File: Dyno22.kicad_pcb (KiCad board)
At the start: 2 copper layers, 160 x 110 mm, 49 parts, among them J2 Display, J3 Pwr Output, J4 BPM & Sensors, J5 Pwr Input, J7 UART, SW1 SW_DPST_x2, U1 TS2937CW50, U2 LM324, U3 74HC4052

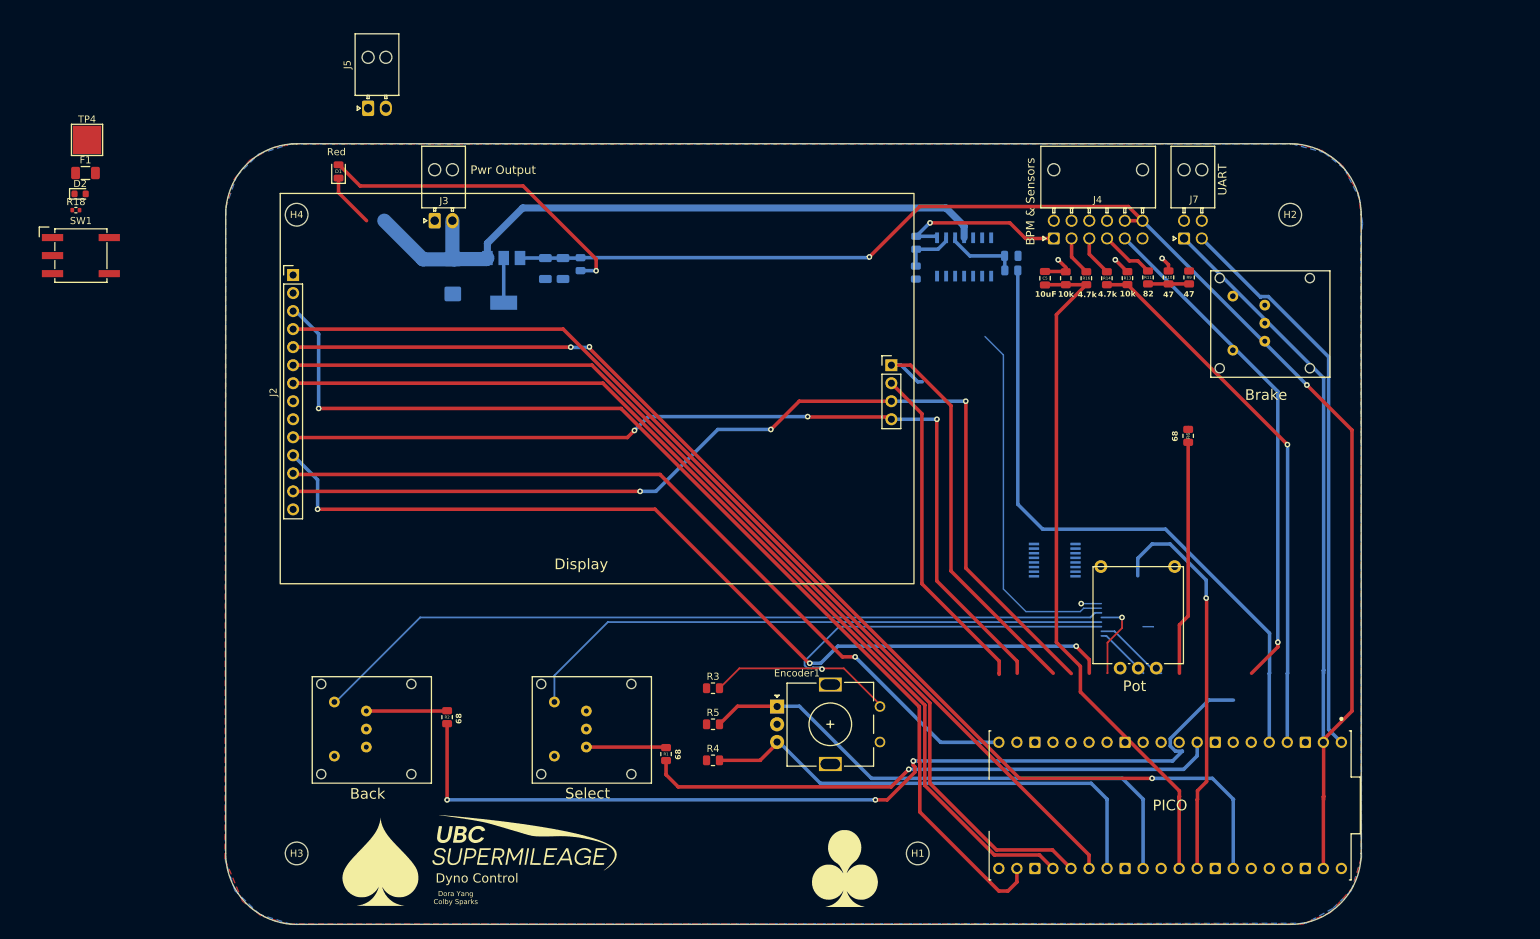
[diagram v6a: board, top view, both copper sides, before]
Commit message: moved LCD PICO, updated traces for buttons encoder pot
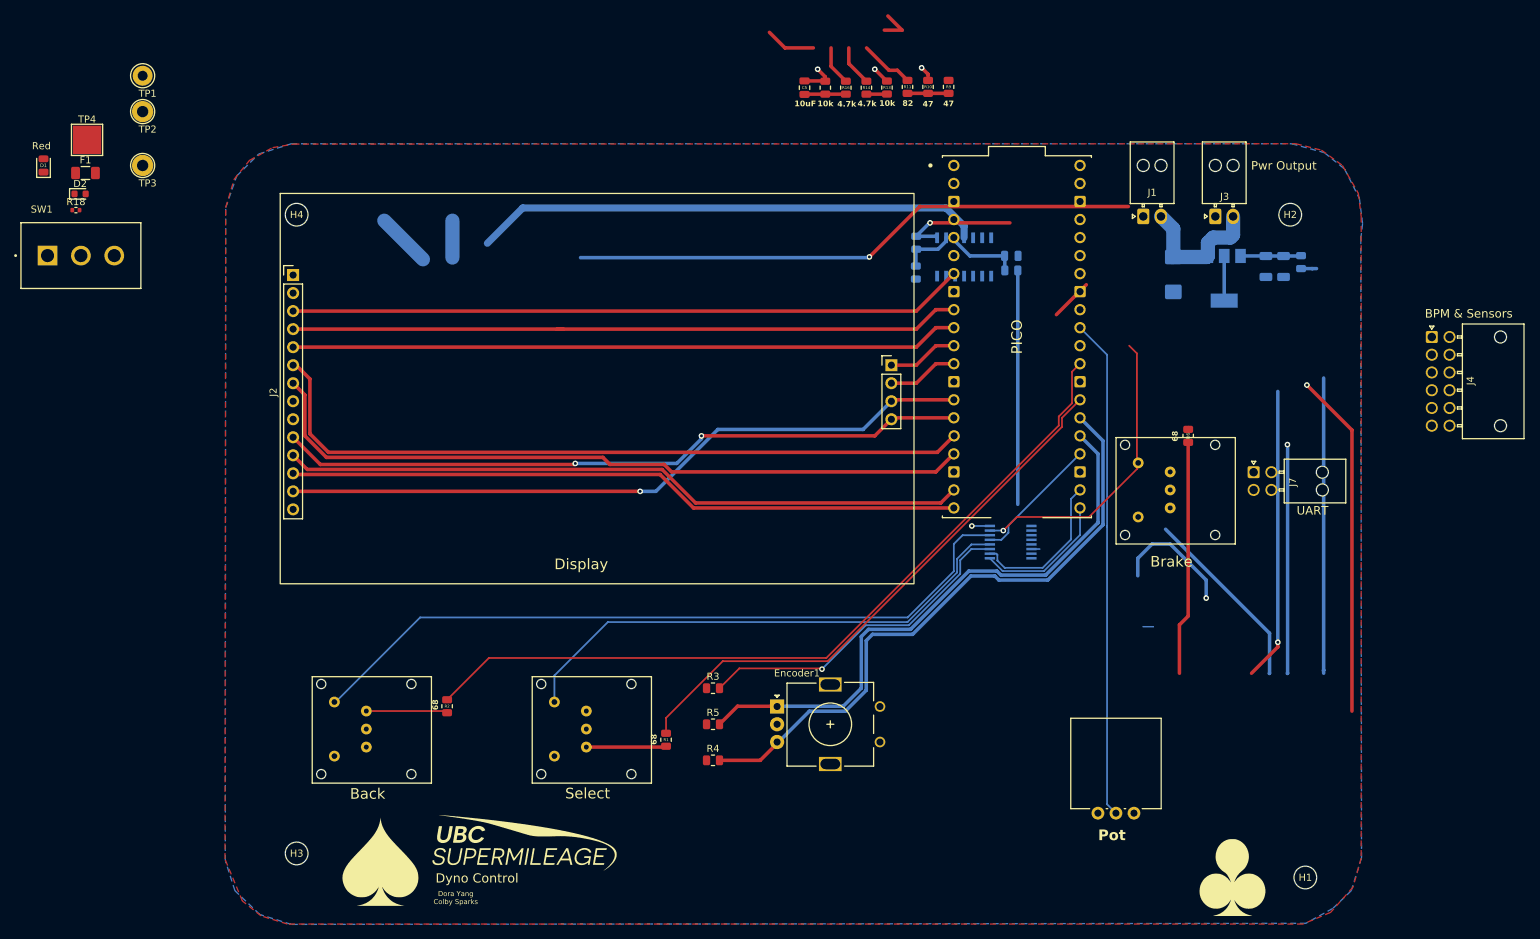
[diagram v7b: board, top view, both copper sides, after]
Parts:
- added TP1: TestPoint 20V, TestPoint:TestPoint_Loop_D2.60mm_Drill1.4mm_Beaded, F.Cu at (50.8, 22.9)
- added TP2: TestPoint 5V, TestPoint:TestPoint_Loop_D2.60mm_Drill1.6mm_Beaded, F.Cu at (50.8, 28.0)
- added TP3: TestPoint 3.3V, TestPoint:TestPoint_Loop_D2.60mm_Drill1.6mm_Beaded, F.Cu at (50.8, 35.6)
- RV1: footprint Potentiometer_THT:Potentiometer_Vishay_148-149_Single_Vertical_1 -> Potentiometer_THT:Potentiometer_Vishay_148-149_Single_Vertical
- SW1: footprint Button_Switch_SMD:Nidec_Copal_SH-7040B -> 300SP1J1BLKM2QE:SW_300SP1J1BLKM2QE
- moved J1 110.3 mm to (191.8, 42.7)
- moved J3 110.0 mm to (201.9, 42.7)
- moved C1 101.5 mm to (211.6, 49.8)
- moved C2 101.5 mm to (196.0, 50.9)
- moved R7 101.5 mm to (214.0, 49.2)
- moved C3 101.5 mm to (209.1, 49.8)
- moved U1 101.5 mm to (203.2, 51.5)
- moved A1 69.5 mm to (174.0, 59.7), turned to 0 degrees
- moved J4 55.0 mm to (232.4, 59.7), turned to 0 degrees
- moved H1 54.7 mm to (214.6, 135.9)
- moved G*** 54.6 mm to (204.5, 135.9)
- moved R14 43.2 mm to (152.8, 24.6)
- moved C5 43.2 mm to (144.1, 24.6)
- moved R13 43.2 mm to (155.7, 24.6)
- moved R16 43.2 mm to (149.9, 24.6)
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- renumbered J5 to J1
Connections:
- A1 pad 31: /FORCE_IN -> /BPM_CTRL_IN
- F1 pad 1: Net-(SW1A-B) -> Net-(SW1-A)
- J1 pad 2: Net-(D2-A) -> +24V
- SW1 pad 1: Net-(D2-A) -> Net-(SW1-A)
- SW1 pad 2: Net-(SW1A-B) -> Net-(D2-A)
- TP4 pad 1: unconnected-(TP4-Pad1) -> Earth
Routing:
- net +5V: track 199.7 -> 94.1 mm, vias 2 -> 1
- net /FORCE_IN: track 97.5 -> 5.84 mm
- net /UART_TX: track 79.9 -> 0.00 mm
- net /LCD_DC: track 168.9 -> 94.2 mm, vias 3 -> 0
- net /KILL_SW: track 71.7 -> 0.00 mm, vias 1 -> 0
- net /MOSI_1: track 162.5 -> 105.1 mm, vias 1 -> 0
- net /LCD_CS: track 152.2 -> 95.3 mm, vias 1 -> 0
- net /SD_CS: track 59.8 -> 9.93 mm
- net /LCD_RST: track 144.7 -> 95.1 mm
- net Net-(S3-L1_Y): track 0.43 -> 49.0 mm, vias 0 -> 1
- net /MISO_1: track 144.5 -> 98.4 mm, vias 3 -> 1
- net +3.3V: track 0.00 -> 43.8 mm, vias 0 -> 2
- net Net-(D1-A): track 45.7 -> 2.21 mm, vias 1 -> 0
- net /MOSI_0: track 145.6 -> 103.7 mm
- net /OP_IN: track 76.8 -> 35.2 mm
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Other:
- board outline removed
- board text added: "Pot"

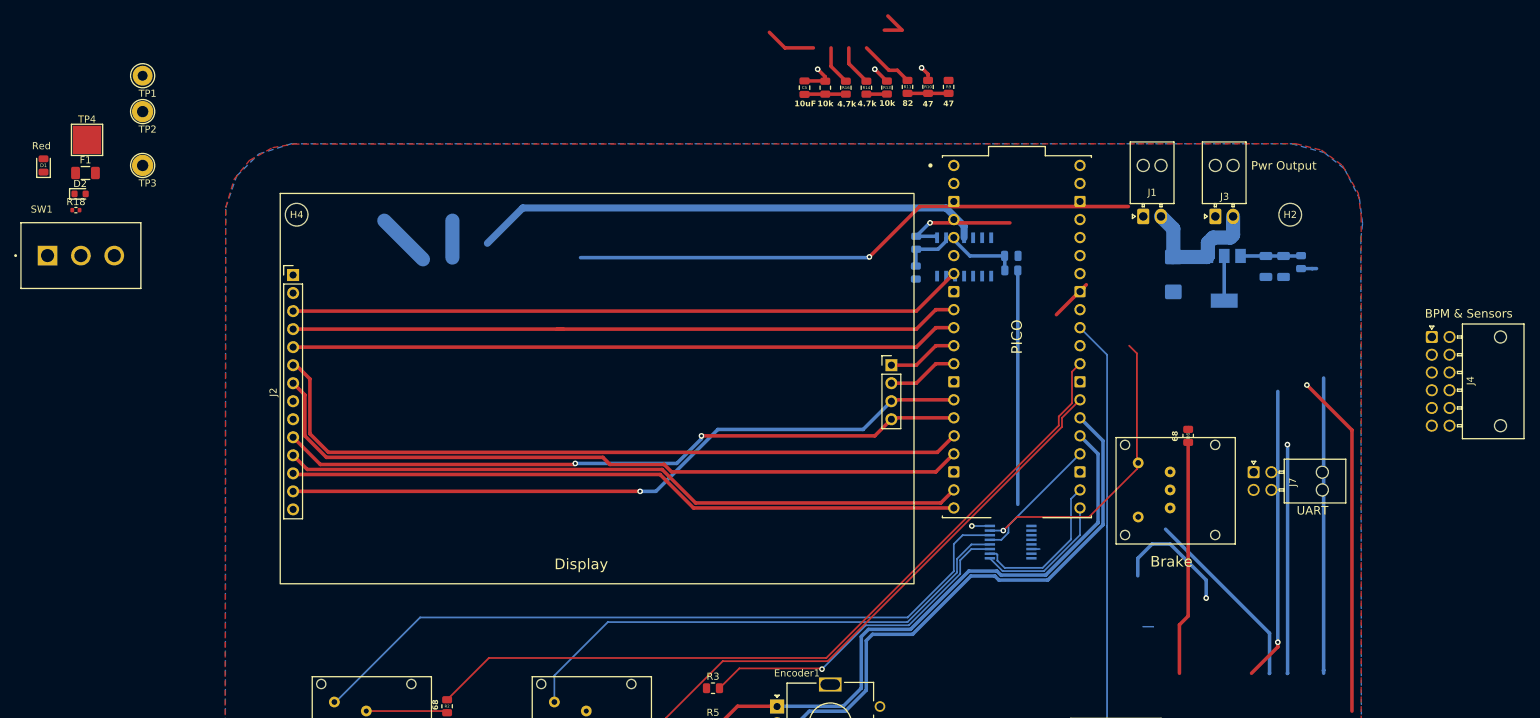
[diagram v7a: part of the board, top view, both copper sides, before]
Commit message: moved components and fixed connections to accomodate for new pico location and power components
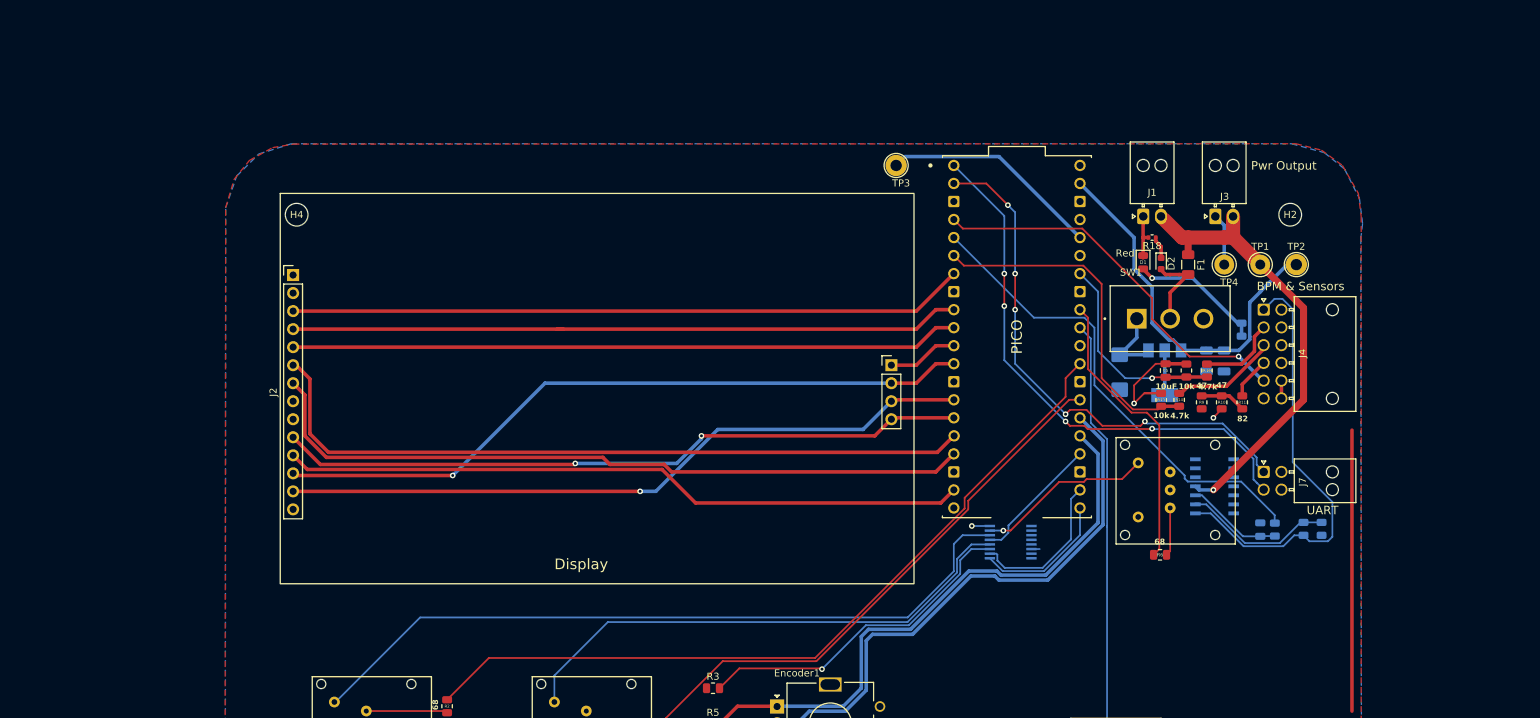
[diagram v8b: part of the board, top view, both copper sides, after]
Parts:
- TP4: footprint TestPoint:TestPoint_Pad_4.0x4.0mm -> TestPoint:TestPoint_Loop_D2.60mm_Drill1.4mm_Beaded
- moved TP2 164.0 mm to (213.4, 49.5)
- moved TP4 161.2 mm to (203.2, 49.5)
- moved TP1 159.7 mm to (208.3, 49.5)
- moved F1 155.9 mm to (198.1, 49.5), turned to -90 degrees
- moved D1 155.5 mm to (191.8, 49.2), turned to -90 degrees
- moved SW1 153.7 mm to (195.6, 57.1)
- moved D2 152.6 mm to (194.3, 49.4), turned to -90 degrees
- moved R18 151.7 mm to (193.0, 45.7), turned to 180 degrees
- moved TP3 106.2 mm to (157.0, 35.6)
- moved R15 67.9 mm to (214.4, 86.8), turned to -90 degrees
- moved R12 67.6 mm to (216.9, 86.8)
- moved R11 64.8 mm to (205.7, 68.9)
- moved C5 64.6 mm to (194.9, 64.5)
- moved R16 64.6 mm to (200.8, 64.5)
- moved R17 64.6 mm to (197.9, 64.5)
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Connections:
- A1 pad 10: /LED_BRAKE -> /LCD_DC
- A1 pad 11: /DEMUX_S0 -> /SD_CS
- A1 pad 12: /DEMUX_S1 -> /MOSI_1
- A1 pad 14: /DEMUX_OUT -> /MISO_1
- A1 pad 15: /TOUCH_CS -> /SCLK_1
- A1 pad 16: /MISO_1 -> /MOSI_0
- A1 pad 17: /SD_CS -> /SCLK_0
- A1 pad 19: /SCLK_1 -> /TOUCH_CS
- A1 pad 20: /MOSI_1 -> /MISO_0
- A1 pad 21: /MISO_0 -> /DEMUX_S1
- A1 pad 22: /LCD_CS -> /DEMUX_S0
- A1 pad 24: /SCLK_0 -> /DEMUX_OUT
- A1 pad 25: /MOSI_0 -> /ROT_EN_A
- A1 pad 26: /LCD_RST -> /ROT_EN_B
- A1 pad 27: /ROT_EN_B -> /LED_SELECT
- A1 pad 29: /ROT_EN_A -> /LED_BACK
- A1 pad 32: /BPM_CTRL_IN -> /LED_BRAKE
- A1 pad 34: /LCD_DC -> /FORCE_IN
- A1 pad 4: /OP_IN -> /KILL_SW
- A1 pad 6: /KILL_SW -> /OP_IN
- A1 pad 7: /LED_BACK -> /LCD_CS
- A1 pad 9: /LED_SELECT -> /LCD_RST
- F1 pad 1: Net-(SW1-A) -> +24V
- F1 pad 2: +24V -> Net-(D2-A)
- SW1 pad 1: Net-(SW1-A) -> +24V
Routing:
- net /UART_TX: track 0.00 -> 76.2 mm, vias 0 -> 4
- net /KILL_SW: track 0.00 -> 54.8 mm, vias 0 -> 1
- net /BPM_CTRL: track 24.1 -> 62.2 mm, vias 1 -> 0
- net +5V: track 94.1 -> 57.0 mm, vias 1 -> 0
- net /UART_RX: track 41.7 -> 75.3 mm, vias 0 -> 5
- net +24V: track 105.1 -> 74.9 mm, vias 0 -> 1
- net /FORCE_IN: track 5.84 -> 29.0 mm, vias 0 -> 1
- net Earth: track 18.7 -> 41.4 mm, vias 3 -> 2
- net /BPM_CTRL_IN: track 88.2 -> 70.5 mm, vias 1 -> 0
- net /BTN_BRAKE: track 42.1 -> 24.9 mm
- net Net-(D1-A): track 2.21 -> 18.1 mm, vias 0 -> 1
- net Net-(U2--): track 7.55 -> 21.2 mm
- net /OP_IN: track 35.2 -> 48.7 mm, vias 1 -> 0
- net Net-(D2-A): track 0.00 -> 11.3 mm
- net +3.3V: track 43.8 -> 33.7 mm, vias 2 -> 1
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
